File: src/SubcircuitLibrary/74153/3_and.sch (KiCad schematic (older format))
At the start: 3 parts, among them U1 PORT, U2 d_and, U3 d_and

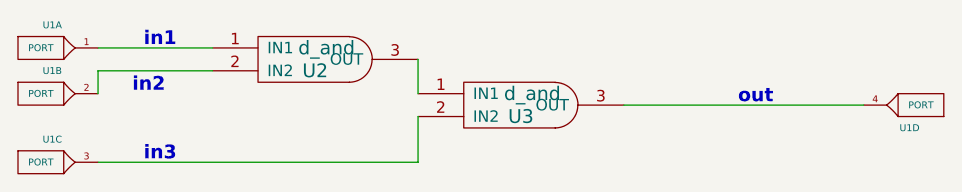
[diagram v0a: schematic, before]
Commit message: common code for Win and Linux, merged py2 changes
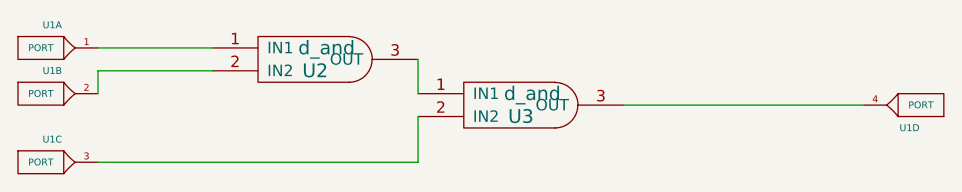
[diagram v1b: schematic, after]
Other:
- note removed: "in1"
- note removed: "in2\n"
- note removed: "in3"
- note removed: "out"
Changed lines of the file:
@@
 LIBS:eSim_Subckt
 LIBS:eSim_User
-LIBS:3_and-cache
 EELAYER 25 0
 EELAYER END
@@
 Wire Wire Line
 	4700 3100 4700 2900
-Text Notes 3500 2600 0    60   ~ 12
-in1
-Text Notes 3450 2800 0    60   ~ 12
-in2\n
-Text Notes 3500 3100 0    60   ~ 12
-in3
-Text Notes 6100 2850 0    60   ~ 12
-out
 $EndSCHEMATC
